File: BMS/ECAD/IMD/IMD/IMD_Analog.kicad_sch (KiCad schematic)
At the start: 106 parts, among them U101 TPSI2140QDWQRQ1, U102 TPSI2140QDWQRQ1, U103 REF2033, U104 AMC3330, U105 TLV6001DCK, U106 AMC3330, U107 TLV6001DCK, U108 TPSI2140QDWQRQ1, U109 TPSI2140QDWQRQ1

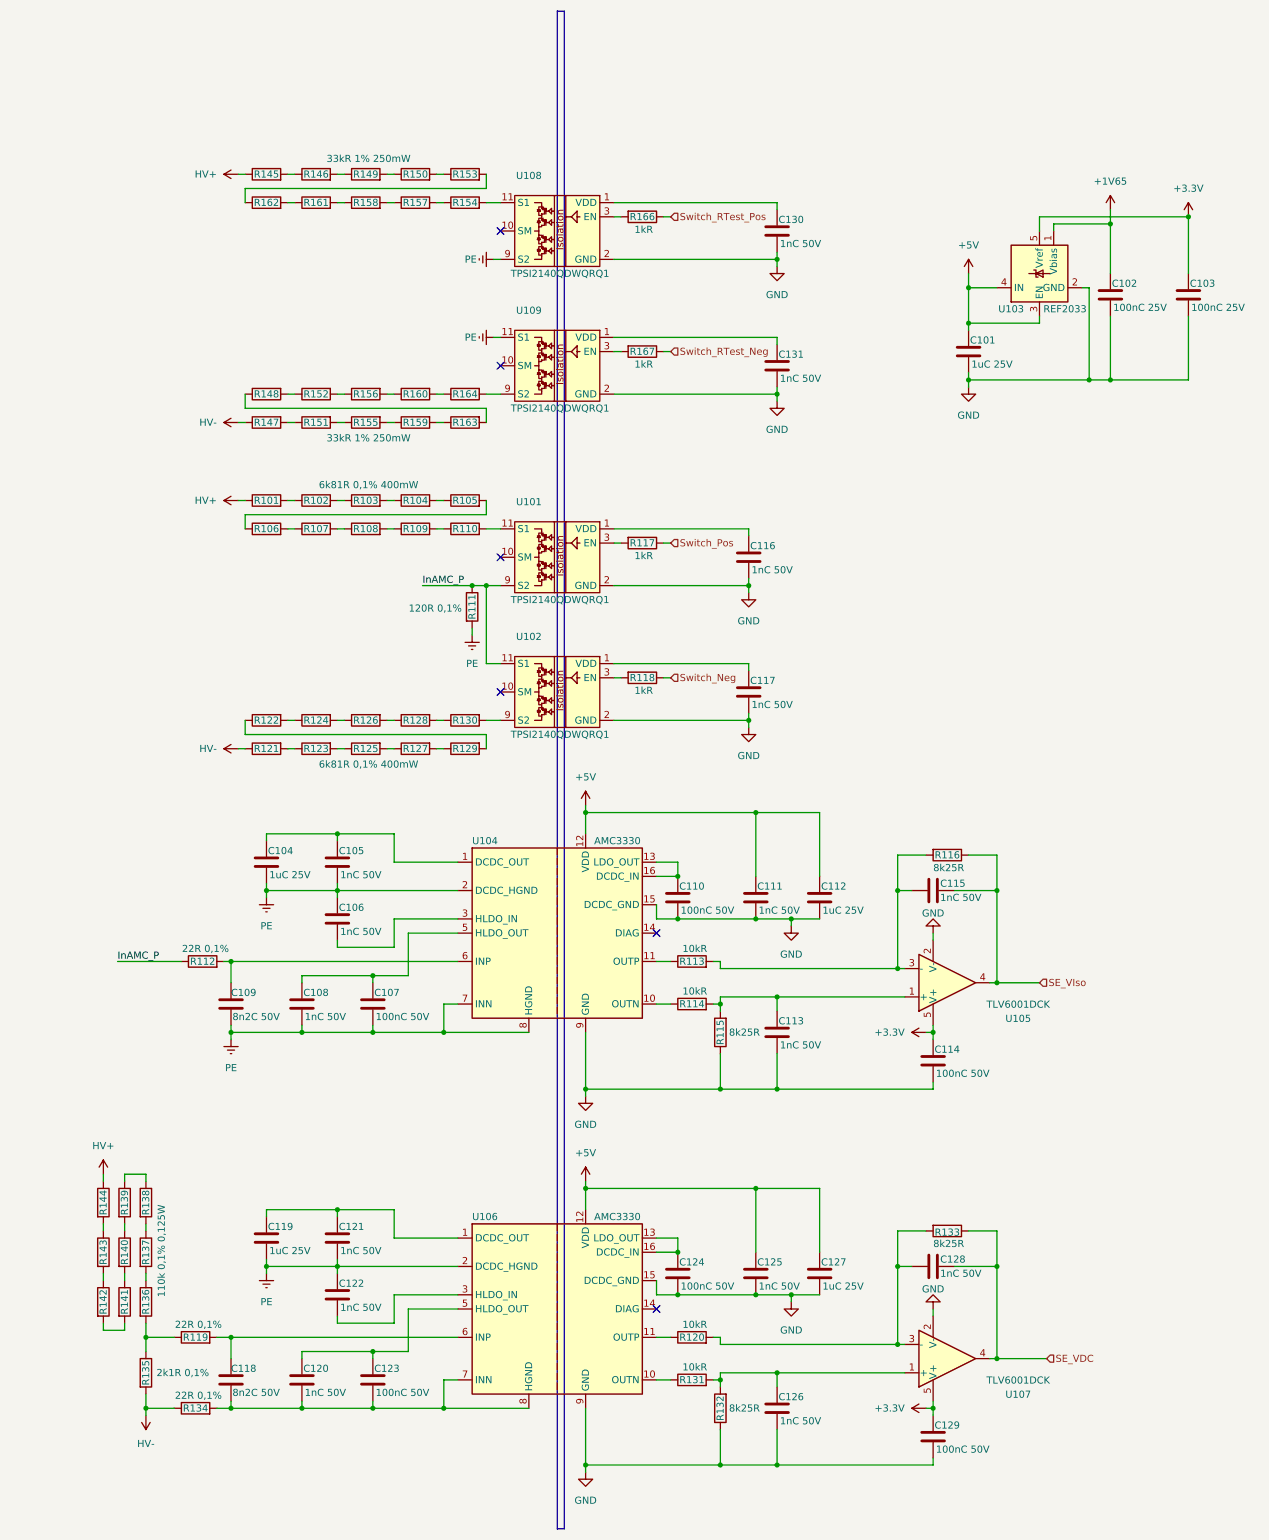
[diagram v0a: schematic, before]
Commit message: add several subcomponent starts
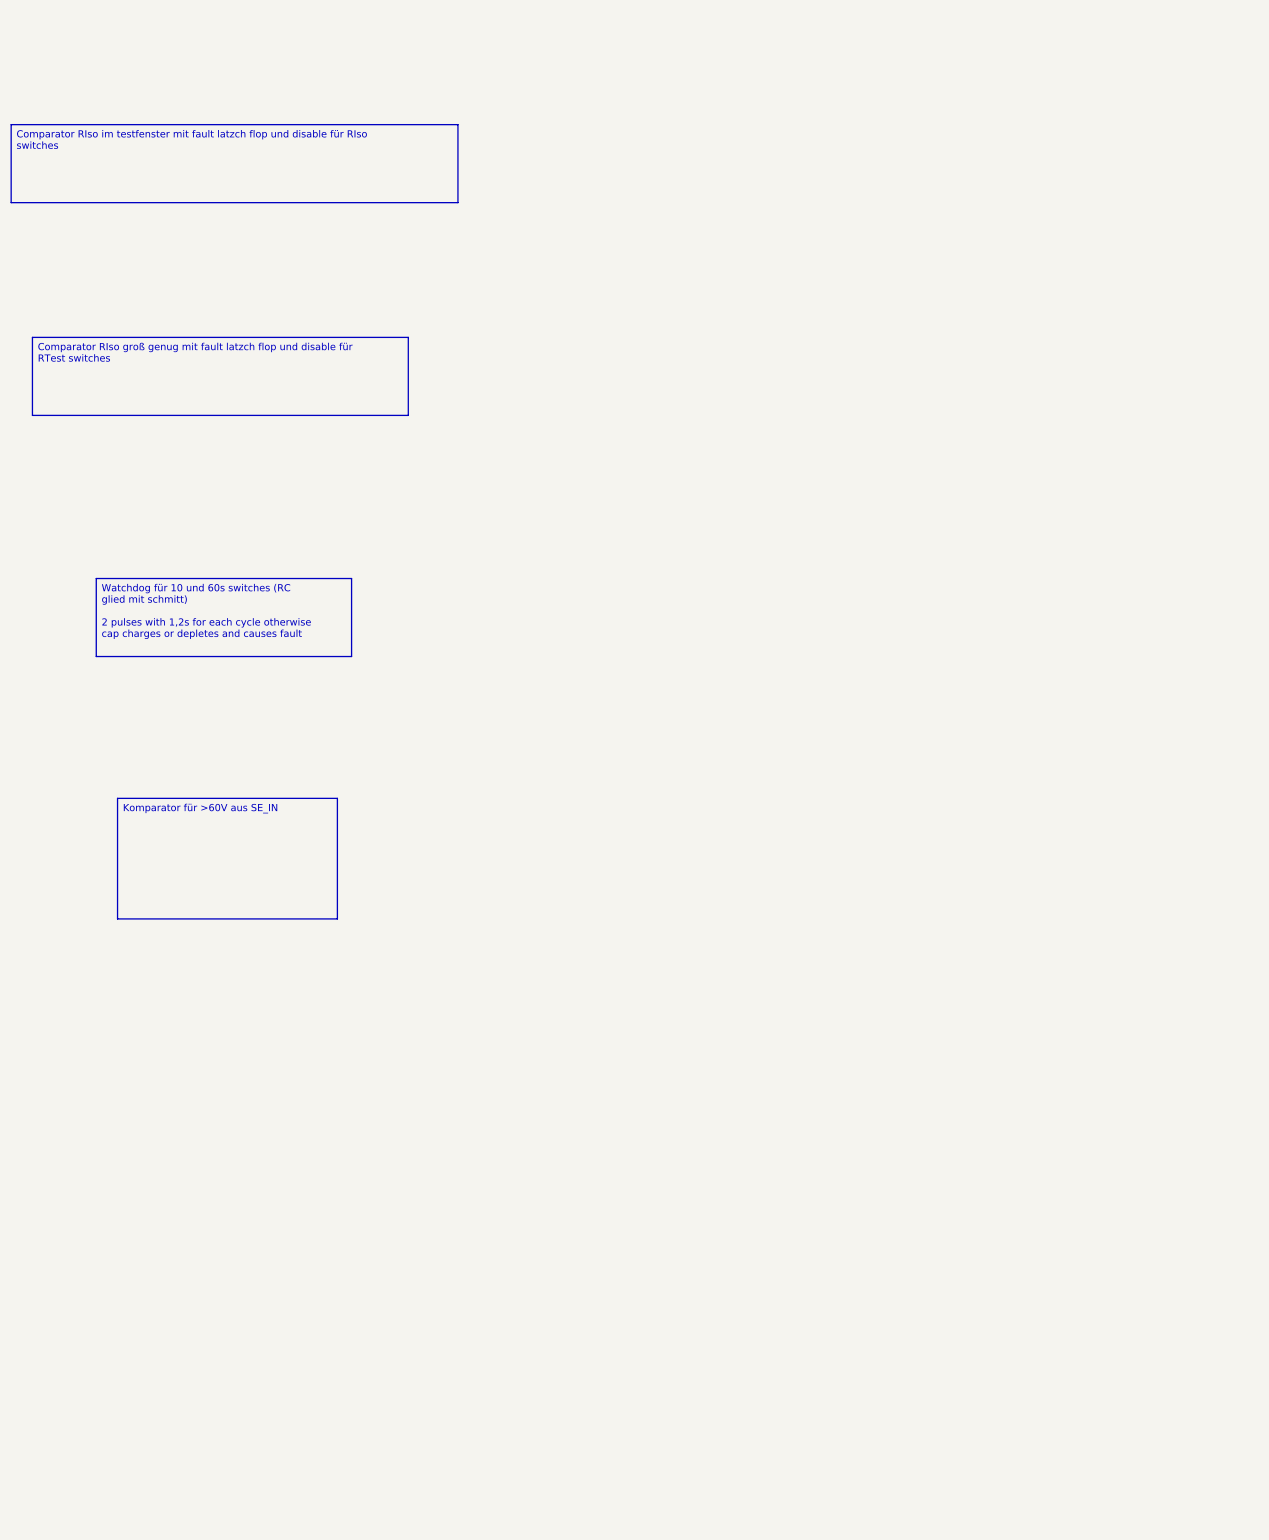
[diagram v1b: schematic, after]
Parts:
- removed C101, C104, C112, C119, C127: 1uC 25V, Capacitor_SMD:C_0603_1608Metric, symbol Device:C
- removed C102, C103: 100nC 25V, Capacitor_SMD:C_0603_1608Metric, symbol Device:C
- removed C105, C106, C108, C111, C113, C115, C116, C117, C120, C121, C122, C125, C126, C128, C130, C131: 1nC 50V, Capacitor_SMD:C_0603_1608Metric, symbol Device:C
- removed C107, C110, C114, C123, C124, C129: 100nC 50V, Capacitor_SMD:C_0603_1608Metric, symbol Device:C
- removed C109, C118: 8n2C 50V, Capacitor_SMD:C_0603_1608Metric, symbol Device:C
- removed R101, R102, R103, R104, R105, R106, R107, R108, R109, R110, R121, R122, R123, R124, R125, R126, R127, R128, R129, R130: 6k81R 0,1% 400mW, Resistor_SMD:R_1206_3216Metric, symbol Device:R
- removed R111: 120R 0,1%, Resistor_SMD:R_0603_1608Metric, symbol Device:R
- removed R112, R119, R134: 22R 0,1%, Resistor_SMD:R_0603_1608Metric, symbol Device:R
- removed R113, R114, R120, R131: 10kR, Resistor_SMD:R_0603_1608Metric, symbol Device:R
- removed R115, R116, R132, R133: 8k25R, Resistor_SMD:R_0603_1608Metric, symbol Device:R
- removed R117, R118, R166, R167: 1kR, Resistor_SMD:R_0603_1608Metric, symbol Device:R
- removed R135: 2k1R 0,1%, Resistor_SMD:R_0603_1608Metric, symbol Device:R
- removed R136, R137, R138, R139, R140, R141, R142, R143, R144: 110k 0,1% 0,125W, Resistor_SMD:R_0805_2012Metric, symbol Device:R
- removed R145, R146, R147, R148, R149, R150, R151, R152, R153, R154, R155, R156, R157, R158, R159, R160, R161, R162, R163, R164: 33kR 1% 250mW, Resistor_SMD:R_0805_2012Metric, symbol Device:R
- removed U101, U102, U108, U109: TPSI2140QDWQRQ1, symbol EKartParts:TPSI2140QDWQRQ1
- removed U103: REF2033, Package_TO_SOT_SMD:SOT-23-5, symbol Reference_Voltage:REF2033
- removed U104, U106: AMC3330, Package_SO:SOIC-16W_7.5x10.3mm_P1.27mm, symbol Isolator_Analog:AMC3330
- removed U105, U107: TLV6001DCK, Package_TO_SOT_SMD:SOT-353_SC-70-5, symbol Amplifier_Operational:TLV6001DCK
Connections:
- no-connect marks 6 -> 0
